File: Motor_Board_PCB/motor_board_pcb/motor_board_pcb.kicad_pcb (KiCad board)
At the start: 2 copper layers, 0.7 x 1.7 mm, 107 parts, among them J1 CAN_OUT, J10 Conn_02x03_Counter_Clockwise, J11 CSP-USC16-TR, J2 Screw_Terminal_01x04, J4 Screw_Terminal_01x14, J5 Conn_02x05_Counter_Clockwise, J6 Barrel_Jack_MountingPin, J7 Screw_Terminal_01x08, J8 Conn_01x02, J9 Conn_02x03_Counter_Clockwise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

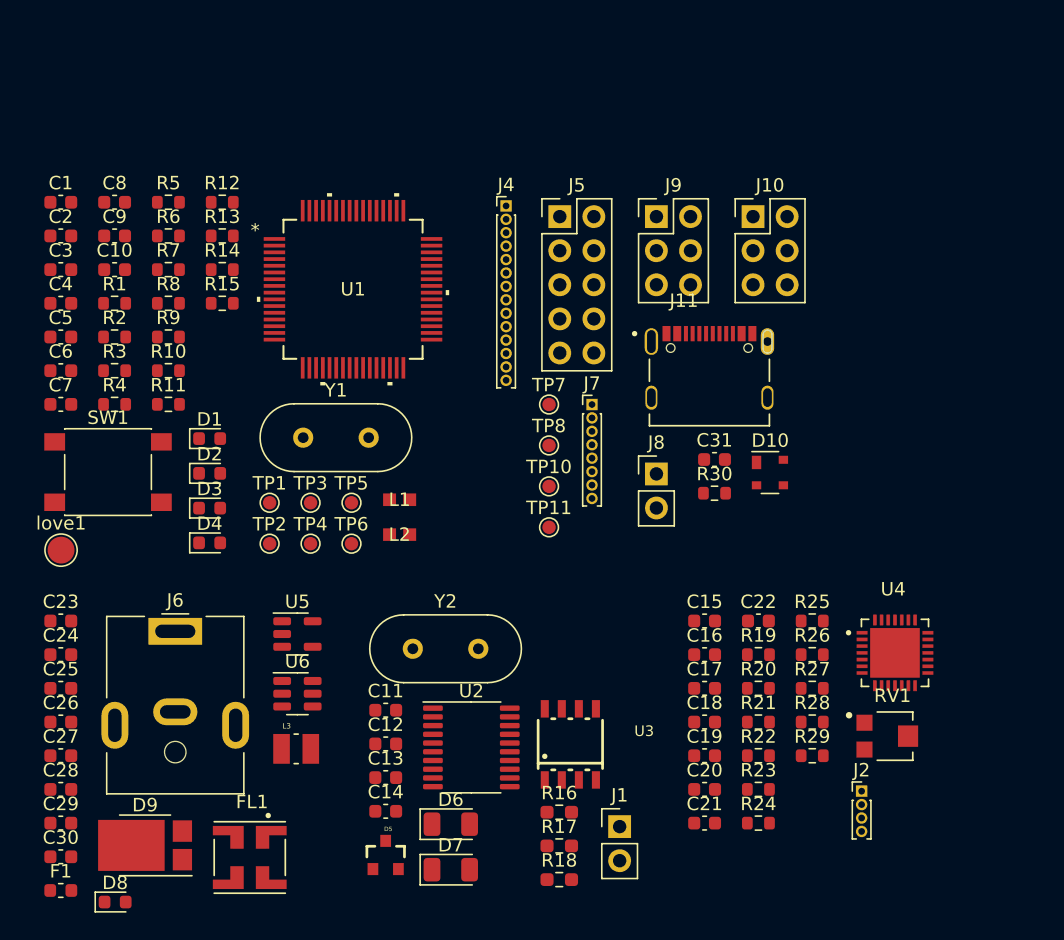
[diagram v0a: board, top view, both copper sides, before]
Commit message: Fixed header sizes
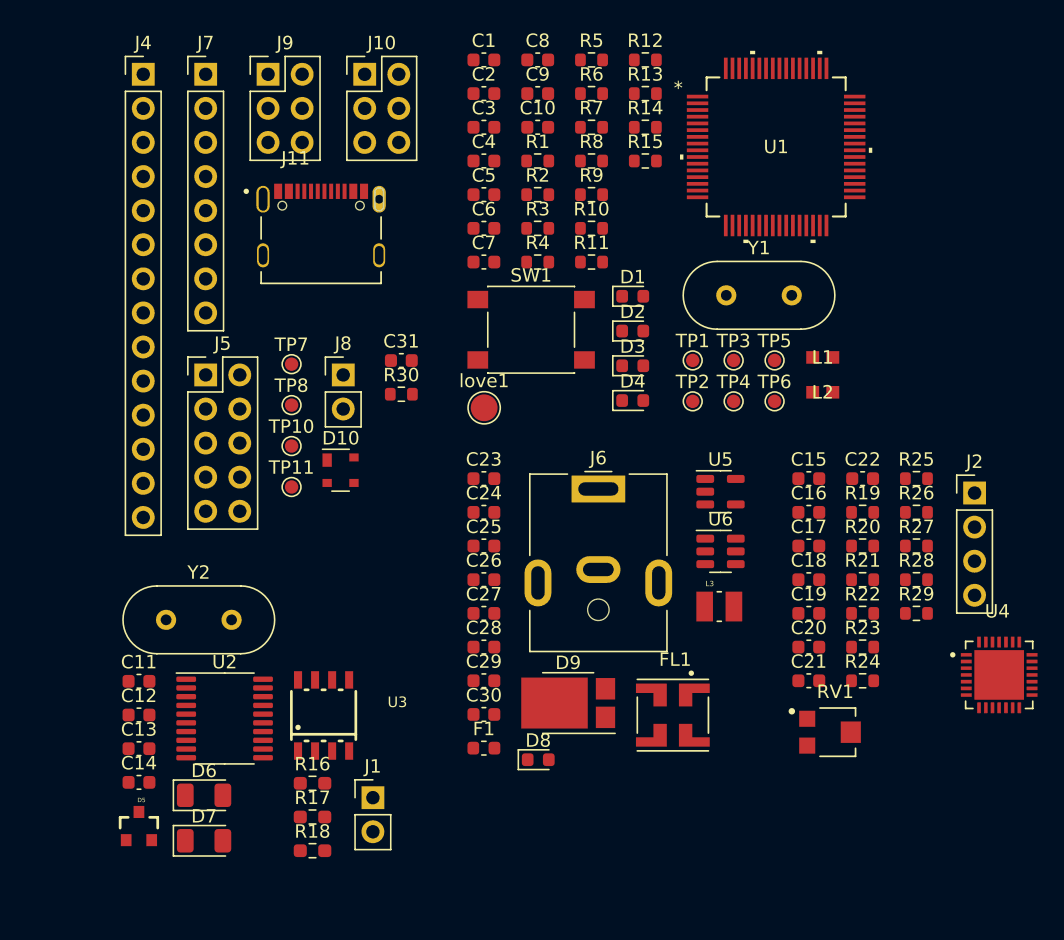
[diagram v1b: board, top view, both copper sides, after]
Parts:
- J2: footprint Connector_PinHeader_1.00mm:PinHeader_1x04_P1.00mm_Vertical -> Connector_PinHeader_2.54mm:PinHeader_1x04_P2.54mm_Vertical
- J4: footprint Connector_PinHeader_1.00mm:PinHeader_1x14_P1.00mm_Vertical -> Connector_PinHeader_2.54mm:PinHeader_1x14_P2.54mm_Vertical
- J7: footprint Connector_PinHeader_1.00mm:PinHeader_1x08_P1.00mm_Vertical -> Connector_PinHeader_2.54mm:PinHeader_1x08_P2.54mm_Vertical
- moved J7 37.9 mm to (123.8, 70.6)
- moved C10 33.3 mm to (148.6, 74.5)
- moved C8 33.3 mm to (148.6, 69.5)
- moved FL1 33.3 mm to (158.7, 118.3)
- moved L1 33.3 mm to (169.8, 91.7)
- moved L2 33.3 mm to (169.8, 94.3)
- moved L3 33.3 mm to (162.1, 110.2)
- moved R1 33.3 mm to (148.6, 77.0)
- moved R10 33.3 mm to (152.6, 82.1)
- moved R11 33.3 mm to (152.6, 84.6)
- moved R3 33.3 mm to (148.6, 82.1)
- moved R4 33.3 mm to (148.6, 84.6)
- moved R5 33.3 mm to (152.6, 69.5)
- moved R7 33.3 mm to (152.6, 74.5)
- moved R8 33.3 mm to (152.6, 77.0)
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
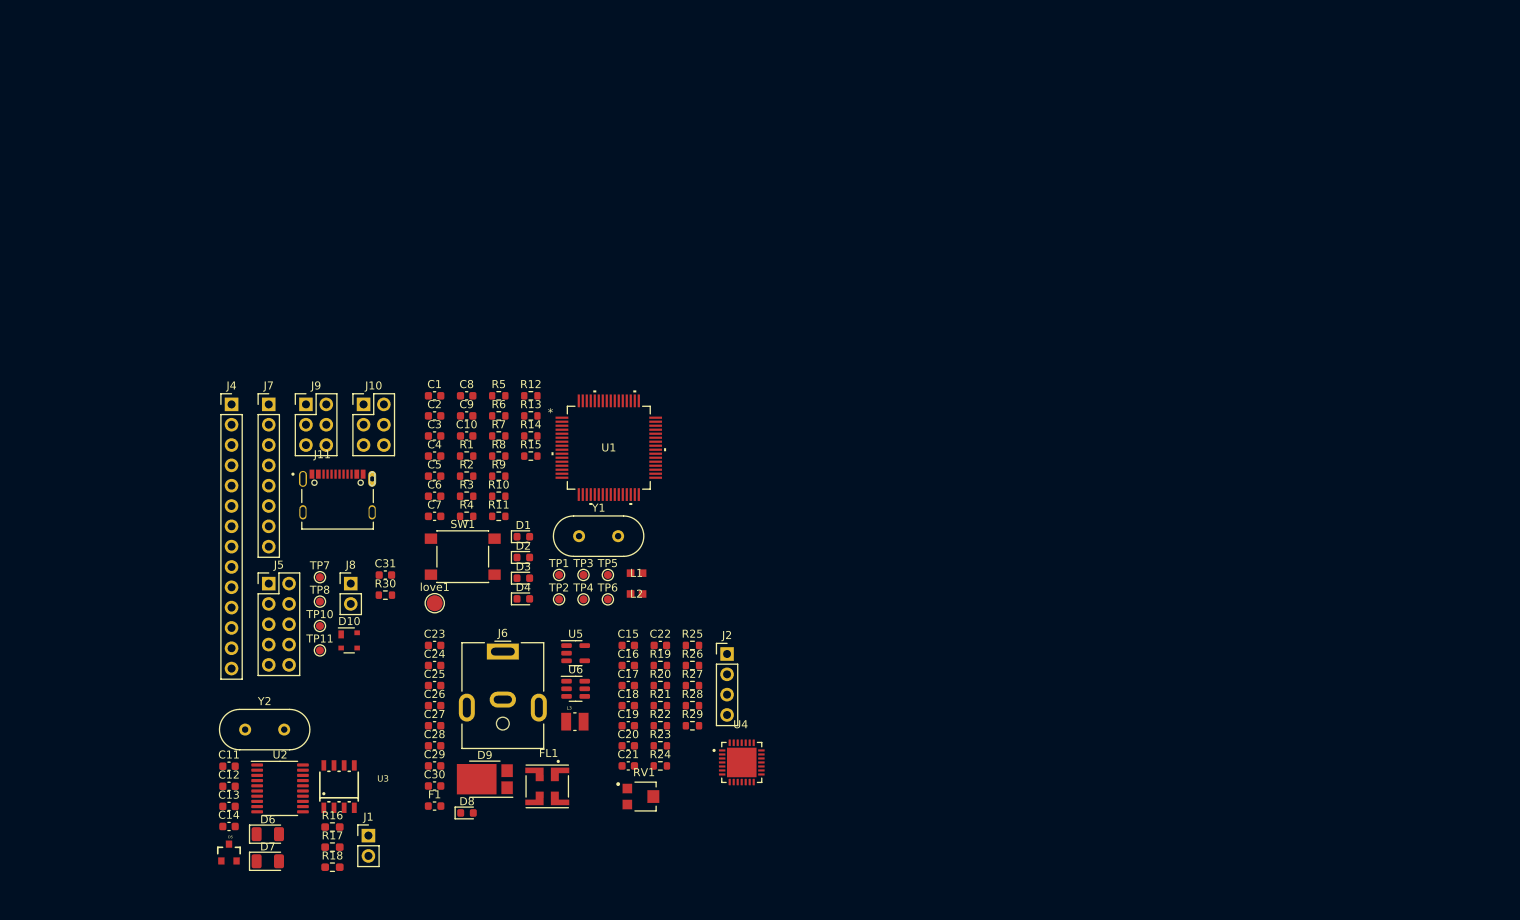
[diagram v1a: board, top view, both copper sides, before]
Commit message: Initial PCB placement for Motor Board
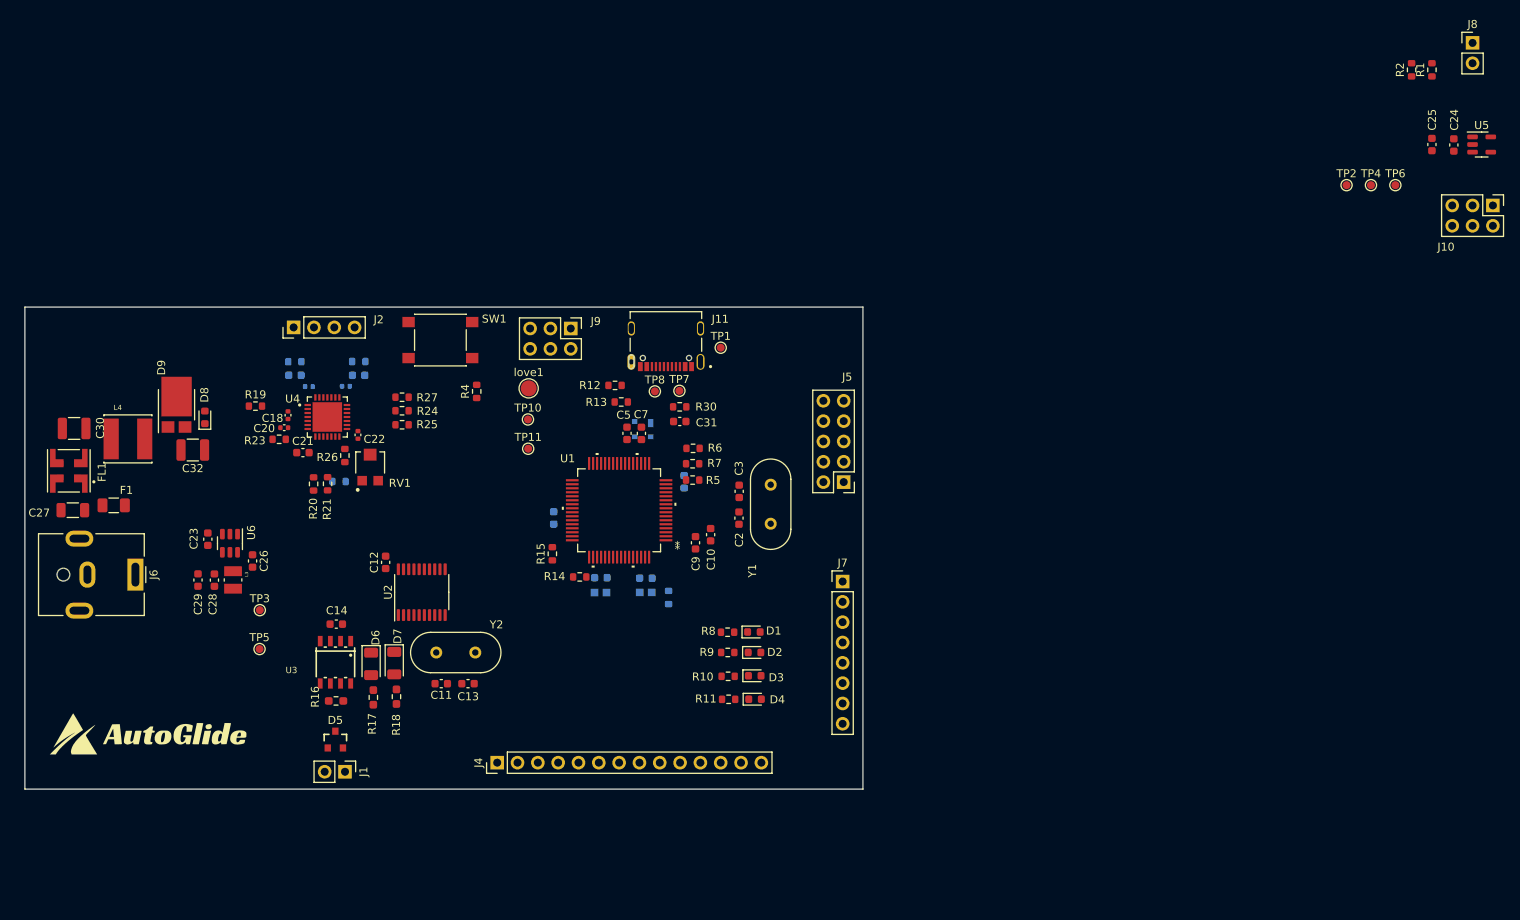
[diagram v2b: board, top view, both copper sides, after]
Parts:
- added C32: 10u, Capacitor_SMD:C_1210_3225Metric, F.Cu at (114.3, 76.3)
- added G***: LOGO, ~ALL:AutoGlideMedium, F.Cu at (109.0, 111.8)
- added L4: VLS6045EX-100M, ~ALL:IND_VLS6045EX-100M, F.Cu at (106.2, 74.9)
- C1, C15, C16, C4, C6, C8, D10, L1, L2, R22, R28, R29, R3: moved to B.Cu
- C17, C19: footprint Capacitor_SMD:C_0603_1608Metric -> Capacitor_SMD:C_0402_1005Metric; moved to B.Cu
- C18, C20, C22: footprint Capacitor_SMD:C_0603_1608Metric -> Capacitor_SMD:C_0402_1005Metric
- C27: value 100u -> 1u; footprint Capacitor_SMD:C_0603_1608Metric -> Capacitor_SMD:C_1206_3216Metric
- C30: value 100u -> 10u; footprint Capacitor_SMD:C_0603_1608Metric -> Capacitor_SMD:C_1210_3225Metric
- F1: footprint Fuse:Fuse_0603_1608Metric -> Fuse:Fuse_1206_3216Metric
- L3: value 4.7u -> DFE252012F-4R7M=P2
- moved J8 155.7 mm to (274.3, 25.4)
- moved J10 143.3 mm to (276.9, 45.7), turned to -90 degrees
- moved C24 143.1 mm to (272.0, 38.2), turned to 90 degrees
- moved C25 141.8 mm to (269.2, 38.1), turned to 90 degrees
- moved R1 130.0 mm to (269.2, 28.8), turned to 90 degrees
- moved U5 129.9 mm to (275.5, 38.1)
- moved R2 128.6 mm to (266.7, 28.8), turned to 90 degrees
- moved TP2 111.2 mm to (258.6, 43.2)
- moved TP4 111.2 mm to (261.6, 43.2)
- moved TP6 111.2 mm to (264.7, 43.2)
- moved J7 75.1 mm to (195.6, 92.7)
- moved J5 73.0 mm to (195.7, 80.3), turned to 180 degrees
- moved FL1 71.6 mm to (98.9, 78.9), turned to -90 degrees
- moved J2 67.8 mm to (127.0, 61.0), turned to 90 degrees
- moved U4 67.4 mm to (131.2, 72.2)
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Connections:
- C12 pad 1: IOREF -> +5V
- C14 pad 1: IOREF -> +5V
- C22 pad 1: IOREF -> +5V
- C24 pad 2: IOREF -> +5V
- C27 pad 1: Net-(D9-K) -> -BATT
- C27 pad 2: -BATT -> Net-(C27-Pad2)
- C28 pad 2: IOREF -> +5V
- C29 pad 2: IOREF -> +5V
- C30 pad 1: +12V -> GND
- C4 pad 2: IOREF -> +5V
- C5 pad 2: IOREF -> +5V
- C6 pad 2: IOREF -> +5V
- D1 pad 2: IOREF -> +5V
- D2 pad 2: IOREF -> +5V
- D3 pad 2: IOREF -> +5V
- D8 pad 1: -BATT -> GND
- D8 pad 2: Net-(D8-A2) -> +12V
- D9 pad 1: Net-(D8-A2) -> Net-(C32-Pad2)
- D9 pad 2: Net-(D8-A2) -> Net-(C32-Pad2)
- D9 pad 3: Net-(D9-K) -> +12V
- F1 pad 2: Net-(D8-A2) -> Net-(C27-Pad2)
- FL1 pad 1: Net-(D9-K) -> Net-(C27-Pad2)
- FL1 pad 2: +12V -> Net-(C30-Pad2)
- FL1 pad 3: Net-(C30-Pad2) -> GND
- J10 pad 1: IOREF -> +5V
- J4 pad 1: IOREF -> +5V
- J5 pad 1: IOREF -> +5V
- J7 pad 1: IOREF -> +5V
- J8 pad 1: IOREF -> +5V
- J9 pad 1: IOREF -> +5V
- L2 pad 2: IOREF -> +5V
- L3 pad 2: IOREF -> +5V
- R12 pad 1: IOREF -> +5V
- R13 pad 1: IOREF -> +5V
- R14 pad 1: IOREF -> +5V
- R17 pad 1: IOREF -> +5V
- R18 pad 1: IOREF -> +5V
- R24 pad 2: D_DIR -> D7
- R25 pad 2: D_STEP -> D6
- R3 pad 1: IOREF -> +5V
- R4 pad 1: IOREF -> +5V
- R5 pad 1: IOREF -> +5V
- TP3 pad 1: IOREF -> +5V
- TP6 pad 1: IOREF -> +5V
- U1 pad 11: IOREF -> +5V
- U1 pad 21: IOREF -> +5V
- U1 pad 39: IOREF -> +5V
- U2 pad 14: CAN_SCK -> D13
- U2 pad 16: CAN_SI -> D11
- U2 pad 17: CAN_SO -> D12
- U2 pad 18: CAN_CS -> D10
- U2 pad 20: IOREF -> +5V
- U3 pad 3: IOREF -> +5V
- U4 pad 15: IOREF -> +5V
- U5 pad 1: IOREF -> +5V
- U5 pad 3: IOREF -> +5V
- U6 pad 1: IOREF -> +5V
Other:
- board size 0.7 x 1.7 mm -> 104.8 x 60.3 mm

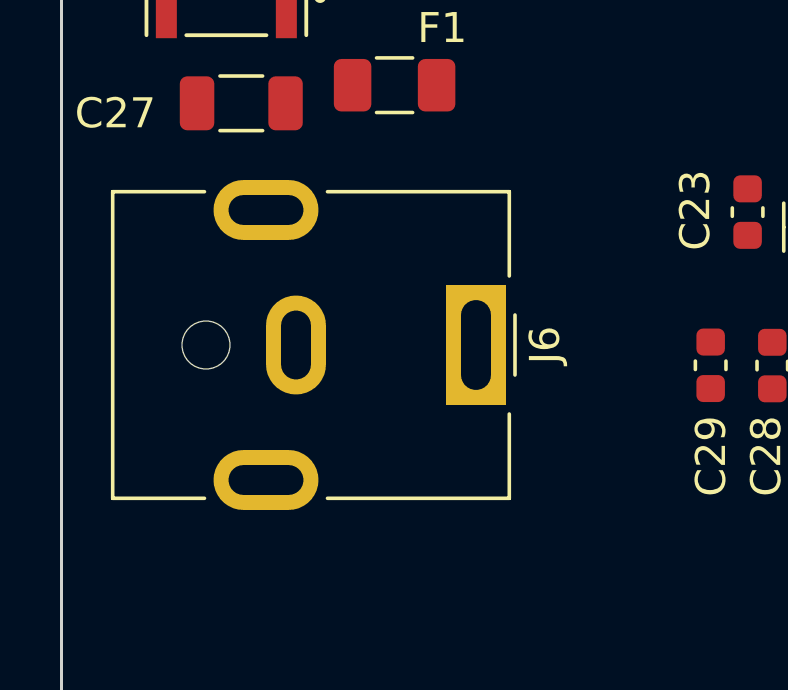
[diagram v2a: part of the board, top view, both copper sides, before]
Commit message: Added cap on accel chip and switched power connector
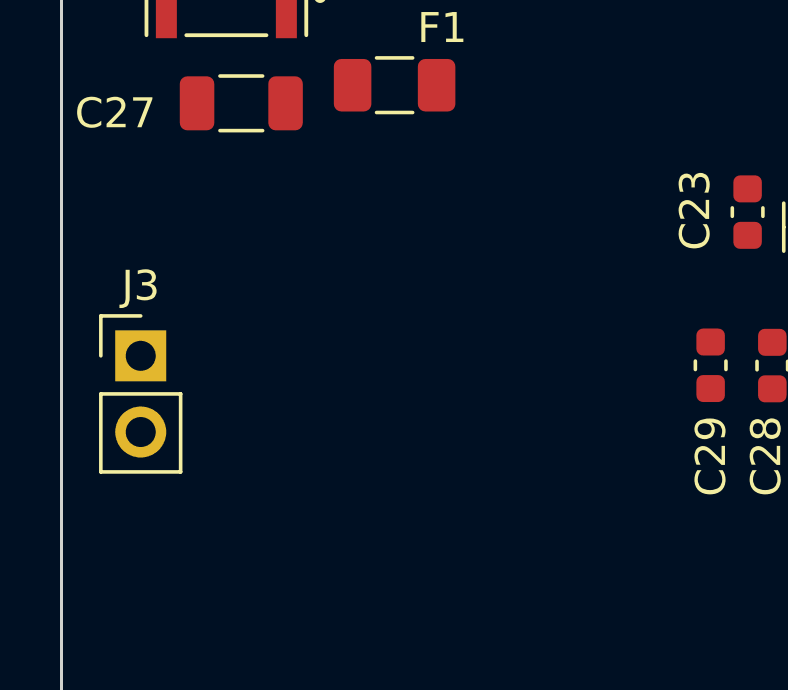
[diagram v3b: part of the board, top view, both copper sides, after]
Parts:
- removed J6: Barrel_Jack_MountingPin, Connector_BarrelJack:BarrelJack_CUI_PJ-063AH_Horizontal
- added J3: Conn_01x02, Connector_PinHeader_2.54mm:PinHeader_1x02_P2.54mm_Vertical, F.Cu at (96.0, 92.2)

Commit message: Meeting Changes
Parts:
- removed C24, C25: 1u, Capacitor_SMD:C_0603_1608Metric
- removed J5: Conn_02x05_Counter_Clockwise, Connector_PinHeader_2.54mm:PinHeader_2x05_P2.54mm_Vertical
- removed J9: Conn_02x03_Counter_Clockwise, Connector_PinHeader_2.54mm:PinHeader_2x03_P2.54mm_Vertical
- removed TP10, TP11: TestPoint, TestPoint:TestPoint_Pad_D1.0mm
- removed U5: AP2112K-3.3TRG1, Package_TO_SOT_SMD:SOT-23-5
- moved J3 134.3 mm to (221.0, 43.2)
- moved TP8 90.5 mm to (254.0, 30.5)
- moved TP7 85.6 mm to (254.0, 35.6)
- moved D5 5.43 mm to (137.6, 111.9)
- moved D6 5.43 mm to (142.0, 102.4)
- moved J1 5.43 mm to (138.8, 115.8)
- moved R16 5.43 mm to (137.6, 107.0)
- moved R17 5.43 mm to (142.3, 106.6)
- moved R18 5.43 mm to (145.2, 106.5)
- moved U2 5.43 mm to (148.4, 93.4)
- moved U3 5.43 mm to (137.6, 102.2)
- moved C12 5.43 mm to (143.8, 89.7)
- moved C14 5.43 mm to (137.7, 97.4)
- moved D7 5.43 mm to (144.9, 102.3)
- moved Y2 5.43 mm to (155.0, 100.9)
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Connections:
- J11 pad A5: /Connectors/CC1 -> CC1
- J11 pad B5: /Connectors/CC2 -> CC2
- J3 pad 1: -BATT -> +BATT
- J3 pad 2: +BATT -> -BATT
- R1 pad 1: /MCU/CC2 -> CC2
- R13 pad 2: /MCU/MD -> BOOT
- R2 pad 1: /MCU/CC1 -> CC1
- U1 pad 26: /MCU/MD -> BOOT

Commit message: Schematic changes before sending to kim
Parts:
- removed J10: Conn_02x03_Counter_Clockwise, Connector_PinHeader_2.54mm:PinHeader_2x03_P2.54mm_Vertical
- removed J7: Screw_Terminal_01x08, Connector_PinHeader_2.54mm:PinHeader_1x08_P2.54mm_Vertical
- removed love1: TestPoint, TestPoint:TestPoint_Pad_D2.0mm
- added D11: PMEG6020AELRX, Diode_SMD:Nexperia_CFP3_SOD-123W, F.Cu at (258.6, 79.0)
- added J5: Screw_Terminal_01x04, Connector_PinHeader_2.54mm:PinHeader_1x04_P2.54mm_Vertical, F.Cu at (246.8, 70.2)
- added J6: Conn_01x03, Connector_PinHeader_2.54mm:PinHeader_1x03_P2.54mm_Vertical, F.Cu at (251.5, 70.2)
- added R31: 10K, Resistor_SMD:R_0603_1608Metric, F.Cu at (257.8, 69.1)
- added R32: 10K, Resistor_SMD:R_0603_1608Metric, F.Cu at (257.8, 71.6)
- added R33: 10K, Resistor_SMD:R_0603_1608Metric, F.Cu at (257.8, 74.1)
- added TP9: TestPoint, TestPoint:TestPoint_Pad_D1.0mm, F.Cu at (246.0, 83.6)
- C1, C5, C6, C9: value 15pF -> 100nF
- C10, C4: value 15pF -> 4.7uF
- C8: value 15pF -> 1uF
- U1: footprint ~ALL:PLQP0064KB-C_REN-M -> R7FA4M1AB3CFM:PLQP0064KB-C_REN
- Y1: value 16MHz? -> 16MHz
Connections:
- U1 pad 24: /MCU/P204 -> unconnected-(U1-GTIOC4B/P204-Pad24)
- U1 pad 32: P300 -> unconnected-(U1-P300/GTIOC0A/TCK/SWCLK-Pad32)
- U1 pad 33: P108 -> unconnected-(U1-P108/GTIOC0B/TMS/SWDIO-Pad33)
- U1 pad 47: A4 -> SDA_Accel
- U1 pad 48: A5 -> SCL_Accel
- U1 pad 50: P501 -> unconnected-(U1-GTIOC2B/AN017/P501-Pad50)
- U1 pad 51: P502 -> unconnected-(U1-GTIOC3B/AN018/P502-Pad51)
- U2 pad 19: unconnected-(U2-~{RESET}-Pad19) -> Net-(U2-~{RESET})
